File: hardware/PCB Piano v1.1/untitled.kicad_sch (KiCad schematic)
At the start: 74 parts, among them U10 MTCH2120-V/SO, U5 MTCH2120-V/SO

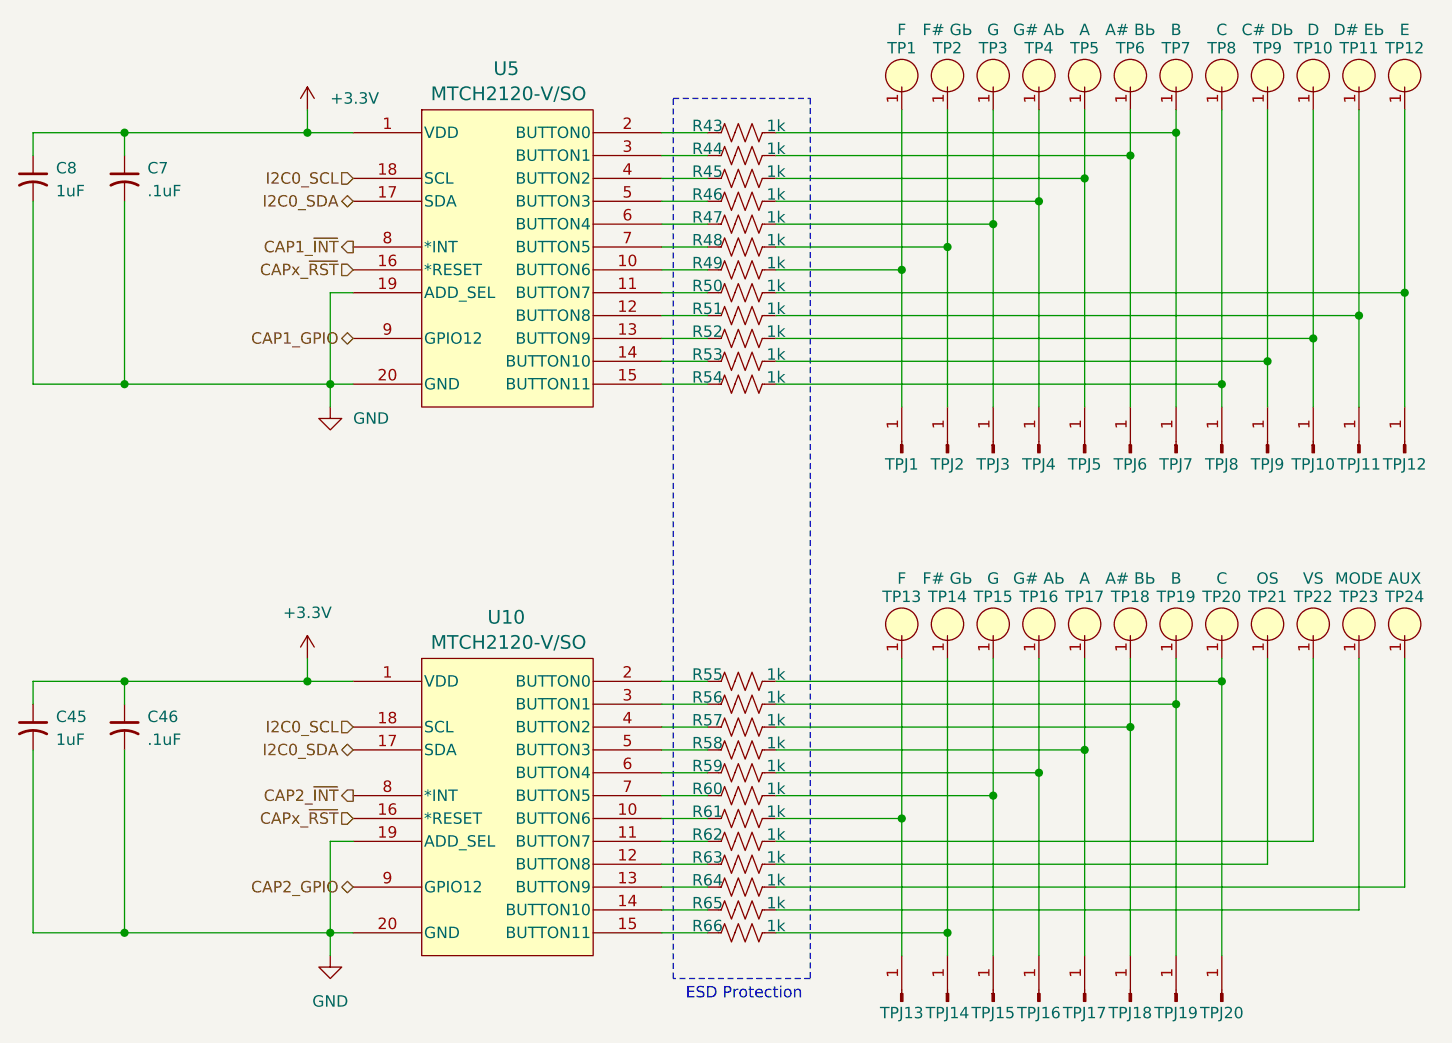
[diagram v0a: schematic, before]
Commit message: Development Phase - PCB Complete - ERC/DRC in progress
Development commit. PBC layout complete. ERC/DRC checks in progress. Swapped some connectors for JST connectors with Adafruit-style polarization.
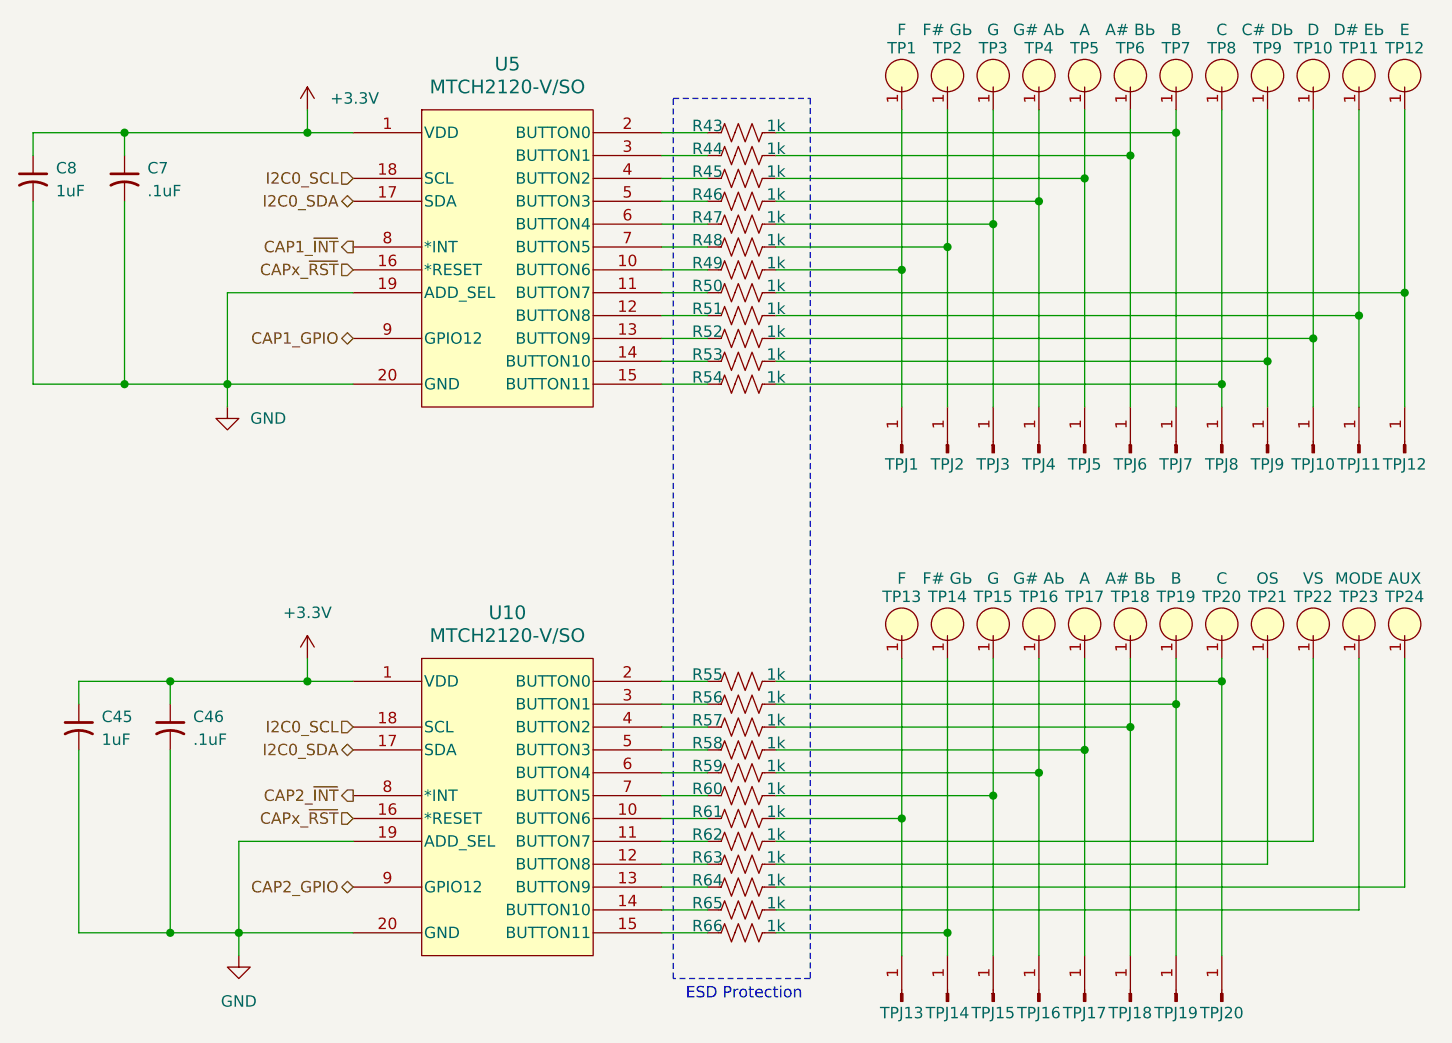
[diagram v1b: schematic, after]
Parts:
- TPJ1, TPJ13: value Conn_01x01_Pin -> F
- TPJ10: value Conn_01x01_Pin -> D
- TPJ11: value Conn_01x01_Pin -> D# Eb
- TPJ12: value Conn_01x01_Pin -> E
- TPJ14, TPJ2: value Conn_01x01_Pin -> F# Gb
- TPJ15, TPJ3: value Conn_01x01_Pin -> G
- TPJ16, TPJ4: value Conn_01x01_Pin -> G# Ab
- TPJ17, TPJ5: value Conn_01x01_Pin -> A
- TPJ18, TPJ6: value Conn_01x01_Pin -> A# Bb
- TPJ19, TPJ7: value Conn_01x01_Pin -> B
- TPJ20, TPJ8: value Conn_01x01_Pin -> C
- TPJ9: value Conn_01x01_Pin -> C# Db
- U10, U5: symbol PCBPiano_Microchip_Symbols:MTCH2120-V_SO -> PCB Piano Symbols:MTCH2120-V_SO
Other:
- moved on the sheet: C45, C46
